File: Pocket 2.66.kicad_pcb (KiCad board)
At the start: 4 copper layers, 45 x 29.2 mm, 74 parts, among them P1 USB-TYPE-C-018, P3 FPC-05F-24PH20, P4 HX-1.25-2AWB, Q1 HL2300, Q2 HL2305, SW1 TS-24CA-S16, SW2 TS-24CA-S16, SW3 TS-24CA-S16, U1 ESP32-C3-MINI-1-N4, U2 LCK-TF-027H30008-WLG, U3 GX4054, U4 GS2019-33TR5, U5 STC3115AIQT, U6 ESD-USB

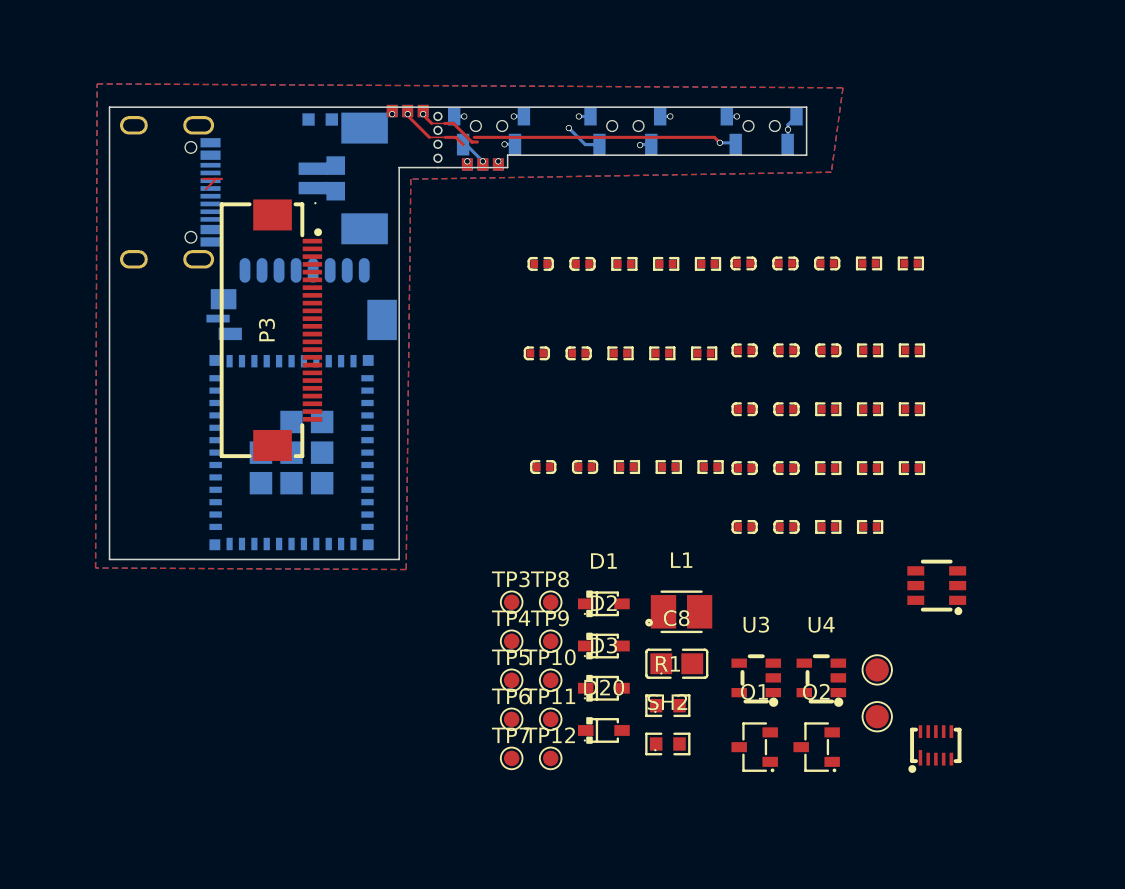
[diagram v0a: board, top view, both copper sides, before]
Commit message: Start of layout with ESP32-C3 mini module
Co-Authored-By: Claude Sonnet 4.6 <noreply@anthropic.com>
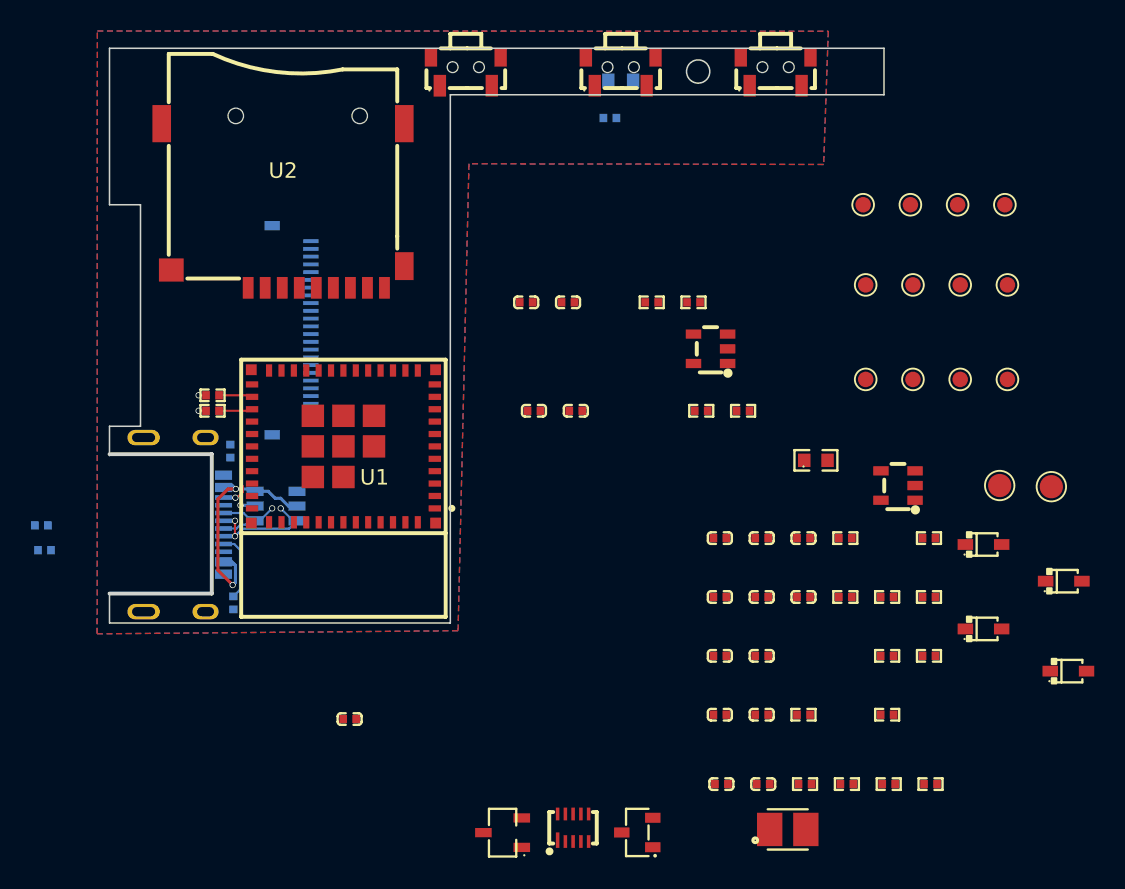
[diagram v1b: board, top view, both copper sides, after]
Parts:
- removed P3: FPC-05F-24PH20, LCSC:C2856805_FPC-SMD_24P-P0_50_FPC-05F-24PH20
- removed P4: HX-1.25-2AWB, LCSC:C52016406_CONN-SMD_2P-P1_25_HX-1_25-2AWB
- added P2: FPC-24-pin, LCSC:C324726_FFC-SMD_24P-P0_50_FH34SRJ-24S-0_5SH, B.Cu at (111.8, 85.2)
- added VBAT1: TestPoint, TestPoint:TestPoint_Pad_D1.0mm, F.Cu at (157.8, 77.1)
- added VBAT2: TestPoint, TestPoint:TestPoint_Pad_D1.0mm, F.Cu at (158.0, 88.4)
- C0, C11, C12, C21, C22, C23: value 4.7uF 10V -> 4.7uF
- C1, C13, C2, C20, C3, C4, C5, C6, C7, C9: value 1uF -> 4.7uF
- C30, C31, R10, R21, R9, U6: moved to B.Cu
- C8: value 4.7uF 25V -> 4.7uF; footprint LCSC:C1779_C0805 -> LCSC:C0402
- D1, D2, D20, D3: value Schottky SOD-323 -> SD103AWS-L SOD-323
- D4: value RED -> LED Yel Side; footprint LCSC:C2286_LED0603-RD -> LCSC:C52675985_LED_Side
- P1: value USB-TYPE-C-018 -> TYPE-C 16P CB1.6 073; footprint LCSC:C2927038_USB-C_SMD-TYPE-C-31-M-12 -> LCSC:C2906290_USB-C-SMD_SHOU_TYPE-C-16P-CB1_6
- Q1: value HL2300 -> AO3401-ED
- Q2: value HL2305 -> AO3400; footprint LCSC:SOT23-3 -> LCSC:SOT-23-L
- R1: value 2.2Ω -> 2.2Ω 0402 ±1%; footprint LCSC:R0603 -> LCSC:R0402
- R11, R12, R13, R14, R18, R19, R2, R3, R4: value 10KΩ -> 47kΩ
- R23, R24, R5, R8: value 10KΩ -> 5.1KΩ
- SW1, SW2, SW3, U1: moved to F.Cu
- U2: value LCK-TF-027H30008-WLG -> MLD-TF PUSH-H18; footprint LCSC:C50380692_TF-SMD_HYCW104-TF08-375B -> LCSC:C52750848_SD-SMD_MLD-TF-PUSH-H18; moved to F.Cu
- moved C30 53.8 mm to (95.8, 99.4), turned to 180 degrees
- moved C31 52.0 mm to (95.6, 97.8), turned to 180 degrees
- moved TP7 44.0 mm to (151.7, 77.1)
- moved U6 43.0 mm to (110.8, 96.5), turned to 180 degrees
- moved TP12 42.5 mm to (158.0, 82.3)
- moved R9 41.8 mm to (107.8, 93.0), turned to 90 degrees
- moved R7 40.5 mm to (106.7, 90.4), turned to 180 degrees
- moved TP10 40.4 mm to (154.8, 77.1)
- moved TP6 38.2 mm to (151.9, 82.3)
- moved TP4 36.2 mm to (148.7, 77.1)
- moved R10 35.5 mm to (108.0, 102.8), turned to 90 degrees
- moved TP9 35.0 mm to (154.9, 82.3)
- moved TP11 34.4 mm to (154.9, 88.4)
- moved R8 33.6 mm to (147.6, 114.5)
- moved R2 31.3 mm to (144.8, 110.0)
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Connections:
- net Net-(D4-A) renamed /LTY
- Q1 pad 1: /GDR -> /PG1
- Q1 pad 2: /RESE -> /VBAT
- Q1 pad 3: /Vx -> /LDO_IN
- Q2 pad 1: /PG1 -> /GDR
- Q2 pad 2: /LDO_IN -> /RESE
- Q2 pad 3: /VBAT -> /Vx
- R11 pad 2: /SD_CS -> /DAT1
- R13 pad 2: /DAT1 -> /SD_CS
- R19 pad 1: Net-(U5-BATD/CD) -> GND
- R19 pad 2: GND -> /BATD
- R2 pad 1: /DIS_CS -> 3V3
- R2 pad 2: 3V3 -> /DIS_CS
- R3 pad 1: /DIS_RS -> 3V3
- R3 pad 2: 3V3 -> /DIS_RS
- R6 pad 1: /U+ -> /USBD-
- R6 pad 2: /USBD+ -> /U-
- R7 pad 1: /USBD- -> /U+
- R7 pad 2: /U- -> /USBD+
- R8 pad 1: /SCL -> 3V3
- R8 pad 2: 3V3 -> /SCL
- U2 pad 10: unconnected-(U2-DET-Pad10) -> GND
- U5 pad 8: Net-(U5-BATD/CD) -> /BATD
- U6 pad 3: unconnected-(U6-Pad3) -> VUSB
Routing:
- net /USBD-: track 0.00 -> 17.6 mm, vias 0 -> 4
- net /BUT2: track 17.1 -> 0.00 mm, vias 1 -> 0
- net VUSB: track 0.00 -> 16.5 mm, vias 0 -> 2
- net /USBD+: track 0.00 -> 15.8 mm, vias 0 -> 2
- net /BOOT: track 14.0 -> 0.00 mm, vias 3 -> 0
- net GND: track 9.16 -> 0.97 mm, vias 10 -> 1
- net /BUT: track 5.56 -> 0.00 mm, vias 2 -> 0
- net /CC1: track 0.00 -> 4.40 mm
- net /U-: track 0.00 -> 2.17 mm
- net /U+: track 0.00 -> 2.17 mm
- net /CC2: track 0.00 -> 1.79 mm, vias 0 -> 1
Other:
- board size 45 x 29.2 mm -> 50 x 37.1 mm
- board text removed: "35Ω: W = 0.5 mm, G = 0.12 mm"
- board text removed: "Bottom edge of 2.13{dblquote} E-ink"
- board text removed: "Break here to move the buttons for 2.66{dblquote} E-ink"
- board text removed: "Top edge of 2.13{dblquote} E-ink"
